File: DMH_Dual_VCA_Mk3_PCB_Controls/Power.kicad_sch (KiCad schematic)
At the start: 30 parts, among them J0 Conn_01x01, J100 IDC_02x05, U1 TL074, U2 TL074, U3 TL074, U4 TL072, U5 LM4040LP-5, U6 LM4040LP-5, U7 TL074, U8 TL074

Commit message: Restarting schematic drawing
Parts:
- removed U1, U2, U3, U7, U8: TL074, Package_DIP:DIP-14_W7.62mm_Socket, symbol Amplifier_Operational:TL074
- removed U4: TL072, Package_DIP:DIP-8_W7.62mm_Socket, symbol Amplifier_Operational:TL072

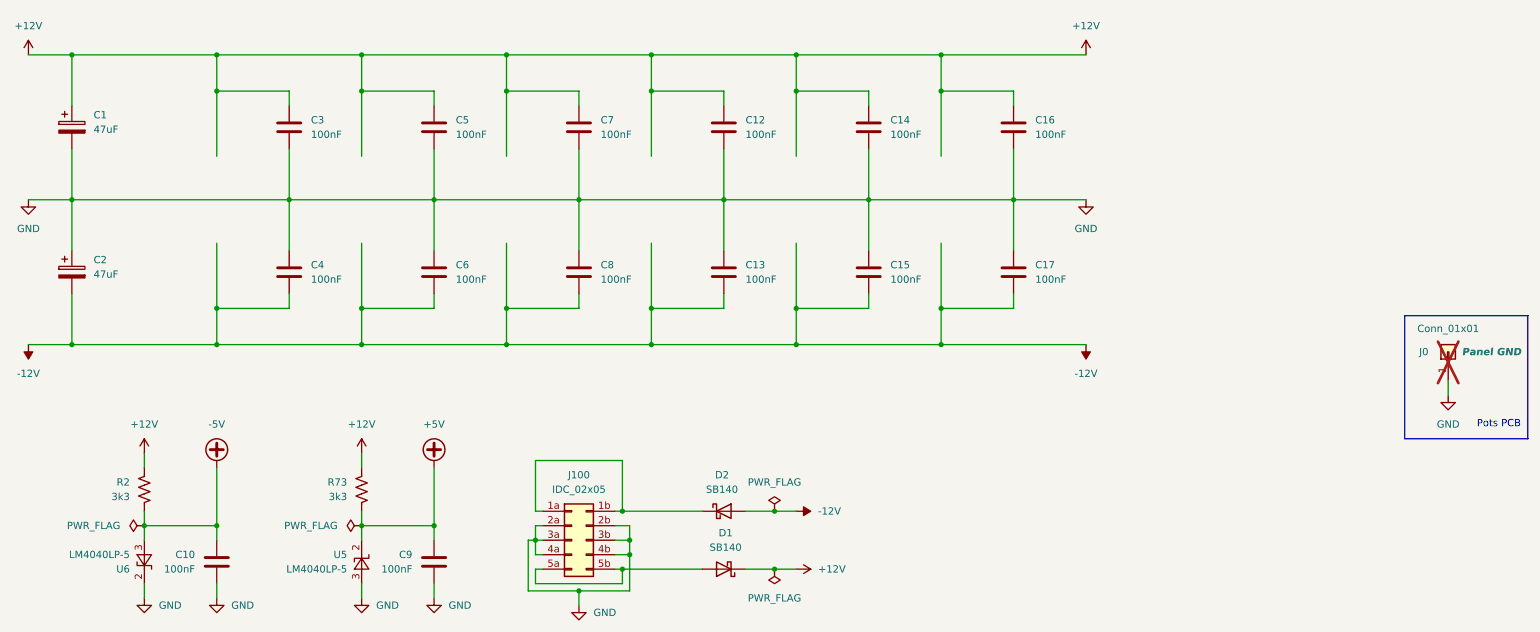
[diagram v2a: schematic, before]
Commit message: Redesigned schematic layout
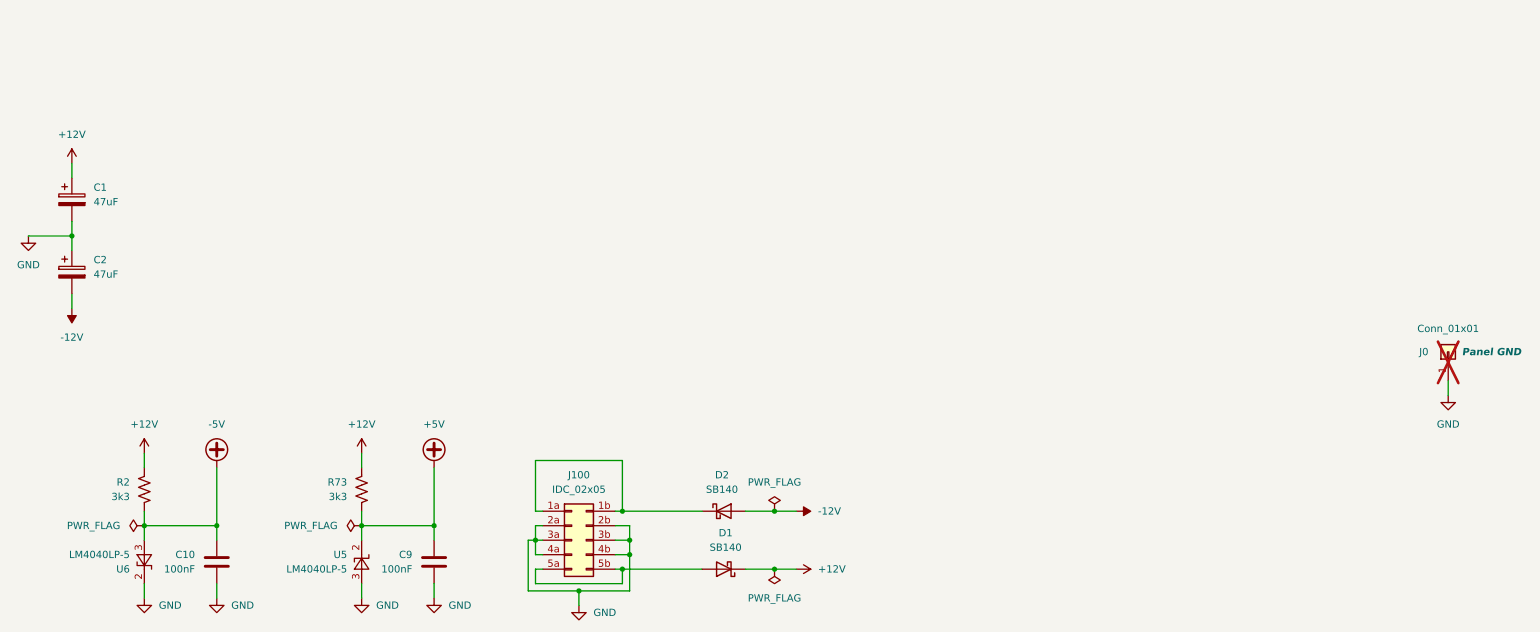
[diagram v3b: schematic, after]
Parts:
- removed C12, C13, C14, C15, C16, C17, C3, C4, C5, C6, C7, C8: 100nF, Capacitor_THT:C_Disc_D4.3mm_W1.9mm_P5.00mm, symbol Device:C
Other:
- note removed: "Pots PCB"
- moved on the sheet: C1
